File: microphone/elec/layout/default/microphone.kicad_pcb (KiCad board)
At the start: 2 copper layers, 40 x 20 mm, 6 parts

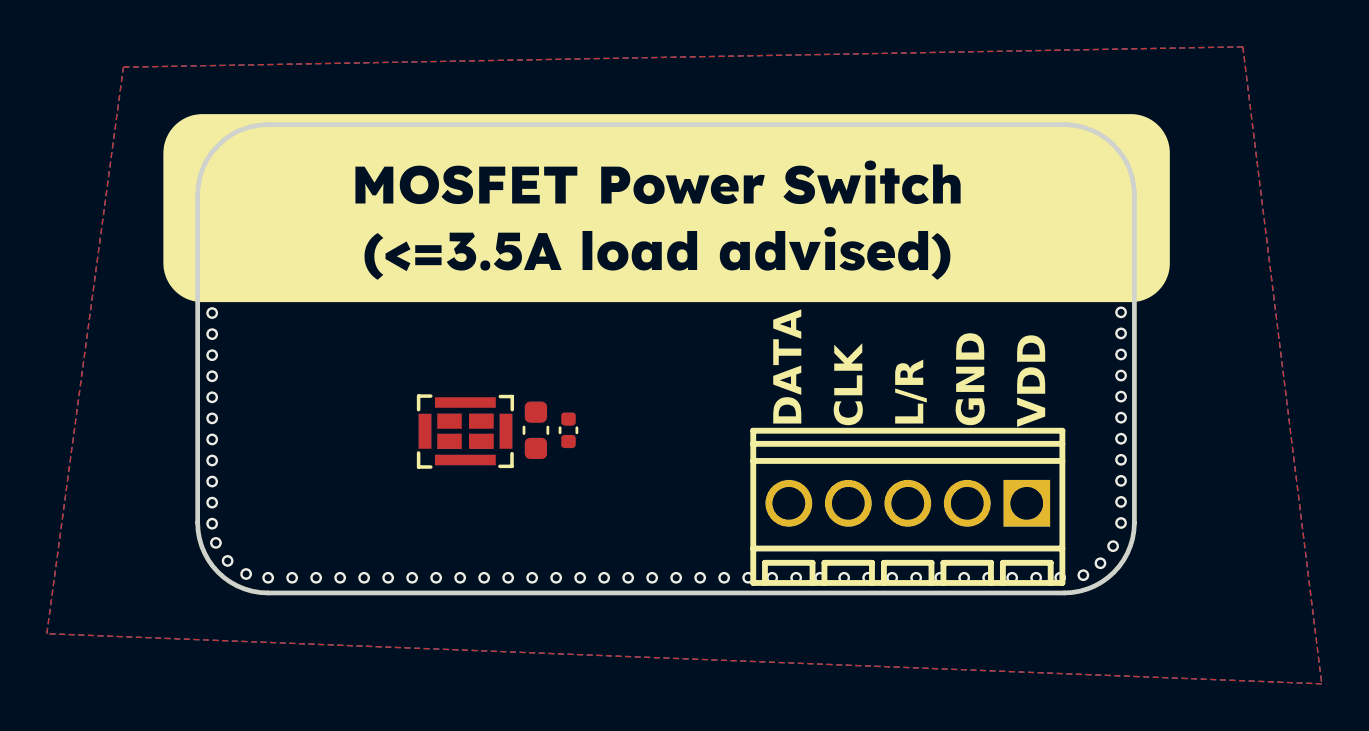
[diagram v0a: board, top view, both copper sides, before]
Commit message: completed mic dev board layouting
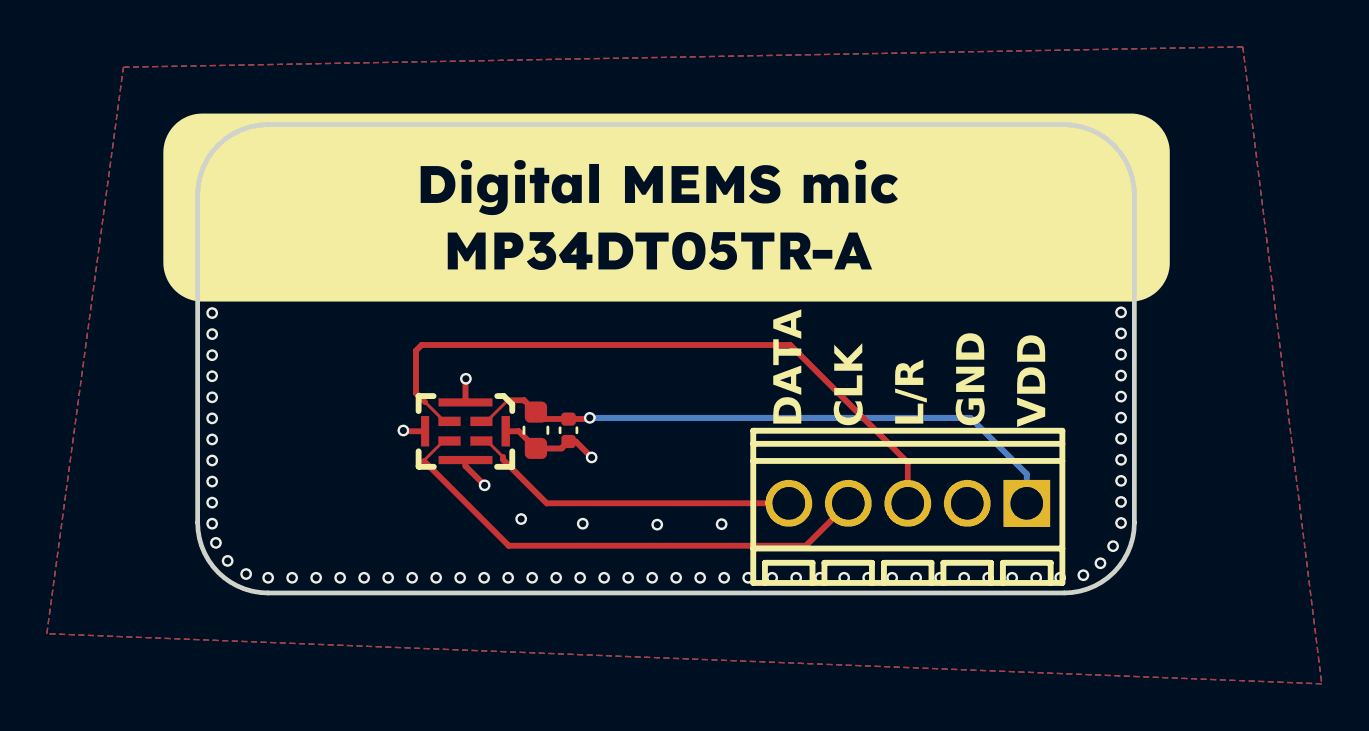
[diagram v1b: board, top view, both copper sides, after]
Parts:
- U1: footprint lib:MIC-SMD_8P-L4.0-W3.0_ZTS6231 -> lib:MIC-SMD_5P-L3.0-W4.0-P0.85-BL
- turned C2 to -90 degrees
- turned U1 to 180 degrees
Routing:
- net l_r: track 0.00 -> 28.7 mm
- net vdd: track 0.00 -> 26.3 mm, vias 0 -> 1
- net clk: track 0.00 -> 21.8 mm
- net data: track 0.00 -> 14.3 mm
- net gnd: track 0.00 -> 7.84 mm, vias 144 -> 152
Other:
- board text added: "bit.ly/3Xj7NgI"
- board text removed: "bit.ly/..."
